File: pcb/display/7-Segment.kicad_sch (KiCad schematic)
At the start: 23 parts, among them J14 XH 2P, J15 XH 2P, J16 XH 2P, J17 XH 2P, J18 XH 2P, J19 XH 2P, J20 XH 2P, Q10 60N03D, Q11 60N03D, Q12 60N03D, Q13 60N03D, Q14 60N03D, Q15 60N03D, Q16 60N03D

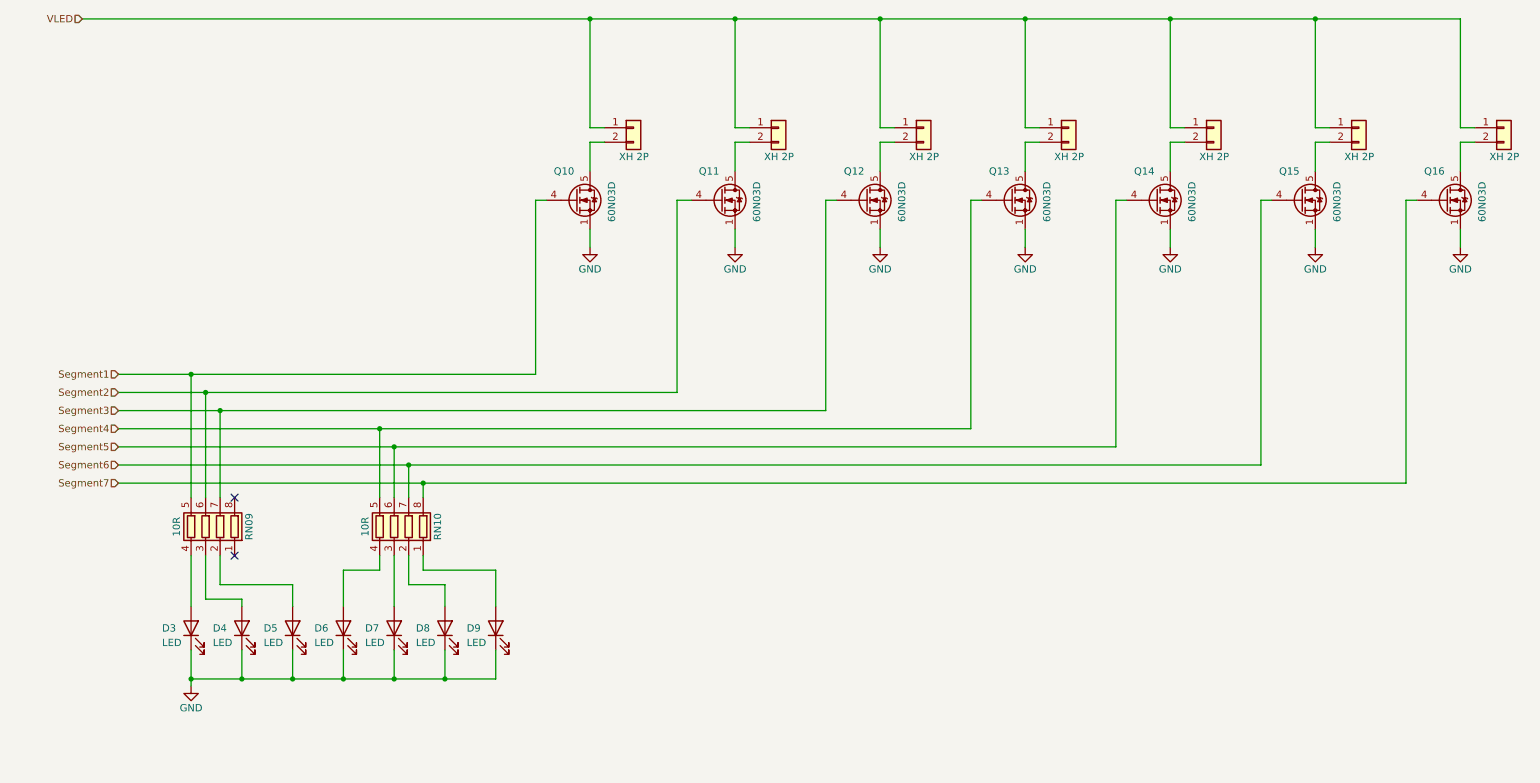
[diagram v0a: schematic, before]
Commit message: Final Version of Prototype Rev. 00
Switched back to PCA9685 for PWM, removed high side switch
Updated some component values
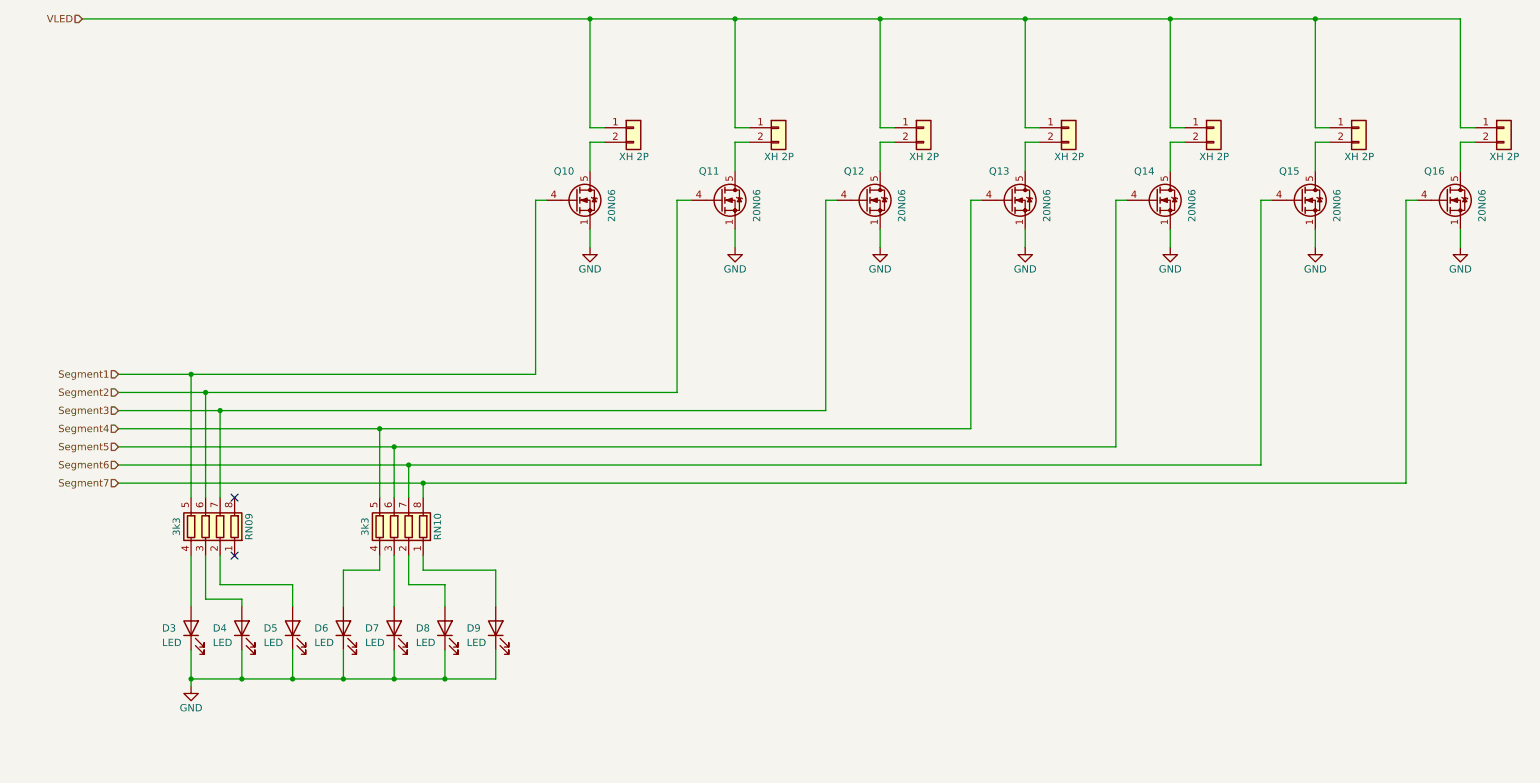
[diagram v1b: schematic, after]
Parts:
- Q10, Q11, Q12, Q13, Q14, Q15, Q16: value 60N03D -> 20N06
- RN09, RN10: value 10R -> 3k3
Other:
- title: (none) -> 7-Segment Driver
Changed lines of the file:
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@@
 	(paper "A4")
 	(title_block
-		(date "2024-11-11")
+		(title "7-Segment Driver")
+		(date "2024-11-17")
 		(rev "00")
 		(company "Ravenspark")
@@
 			)
 		)
-		(property "Value" "60N03D"
+		(property "Value" "20N06"
 			(at 143.51 54.61 90)
 			(effects
@@
 			)
 		)
-		(property "Value" "60N03D"
+		(property "Value" "20N06"
 			(at 168.91 54.61 90)
 			(effects
@@
 			)
 		)
-		(property "Value" "60N03D"
+		(property "Value" "20N06"
 			(at 245.11 54.61 90)
 			(effects
@@
 			)
 		)
-		(property "Value" "60N03D"
+		(property "Value" "20N06"
 			(at 219.71 54.61 90)
 			(effects
@@
 			)
 		)
-		(property "Value" "60N03D"
+		(property "Value" "20N06"
 			(at 270.51 54.61 90)
 			(effects
@@
 			)
 		)
-		(property "Value" "10R"
+		(property "Value" "3k3"
 			(at 74.93 107.95 90)
 			(effects
@@
 			)
 		)
-		(property "Value" "10R"
+		(property "Value" "3k3"
 			(at 41.91 107.95 90)
 			(effects
@@
 			)
 		)
-		(property "Value" "60N03D"
+		(property "Value" "20N06"
 			(at 194.31 54.61 90)
 			(effects
@@
 			)
 		)
-		(property "Value" "60N03D"
+		(property "Value" "20N06"
 			(at 118.11 54.61 90)
 			(effects

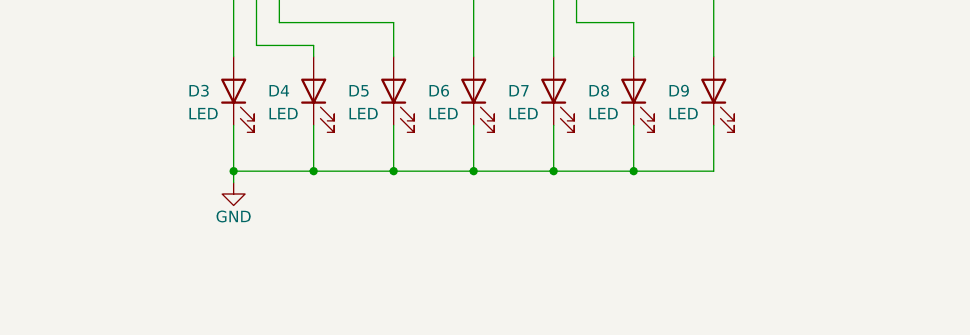
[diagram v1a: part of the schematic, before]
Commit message: Marked known issues in schematic
Add gitignore
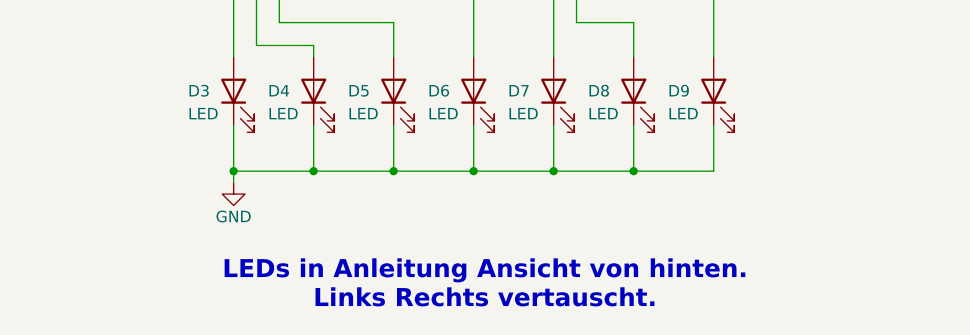
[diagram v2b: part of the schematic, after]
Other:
- note added: "LEDs in Anleitung Ansicht von hinten. Links Rechts vertauscht."
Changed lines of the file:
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@@
+		)
+	)
+	(text "LEDs in Anleitung Ansicht von hinten.\nLinks Rechts vertauscht."
+		(exclude_from_sim no)
+		(at 72.39 147.32 0)
+		(effects
+			(font
+				(size 2 2)
+				(thickness 0.4)
+				(bold yes)
+				(color 255 153 0 1)
+			)
 		)
 	)

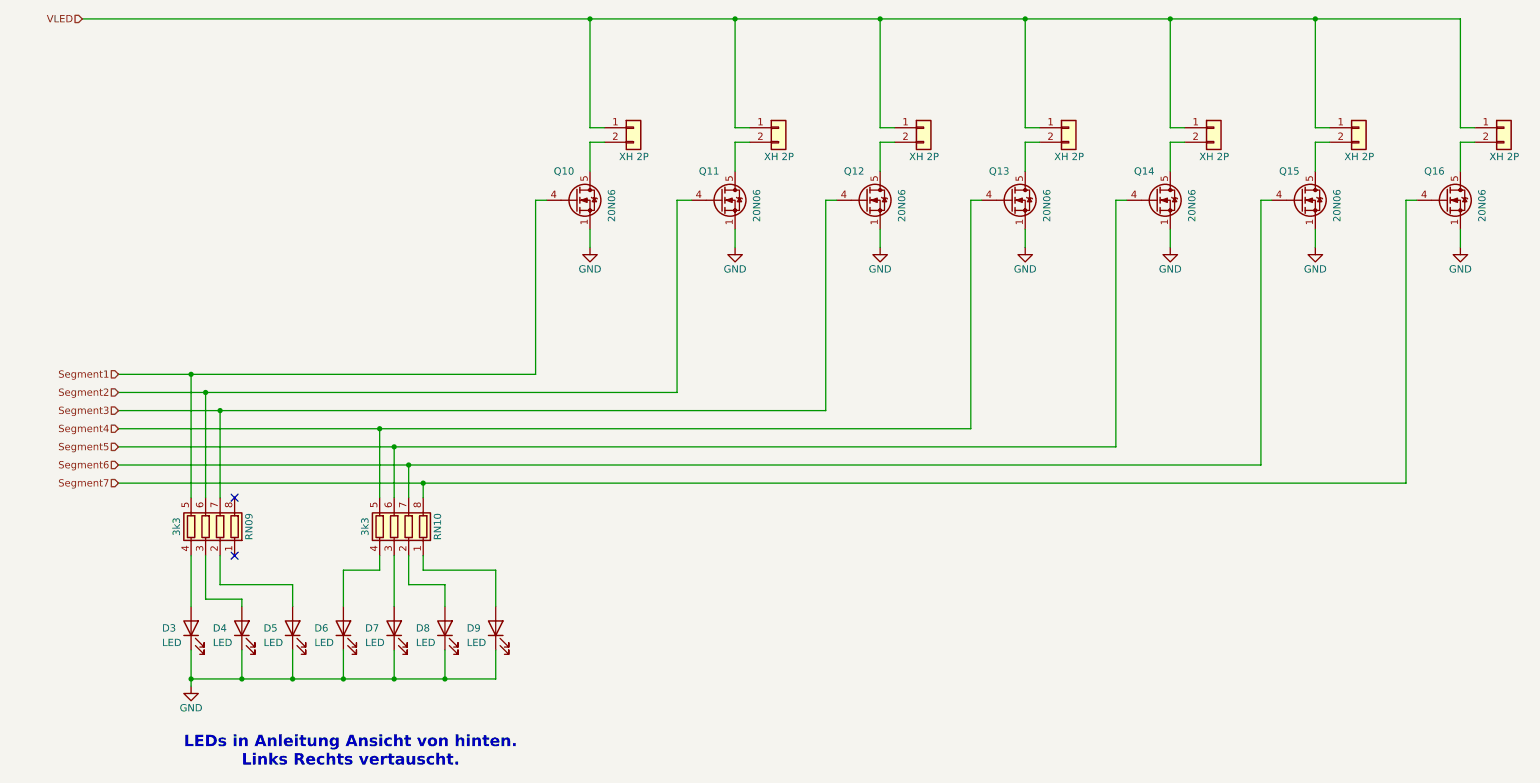
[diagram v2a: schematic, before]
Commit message: Display HW Revision 01
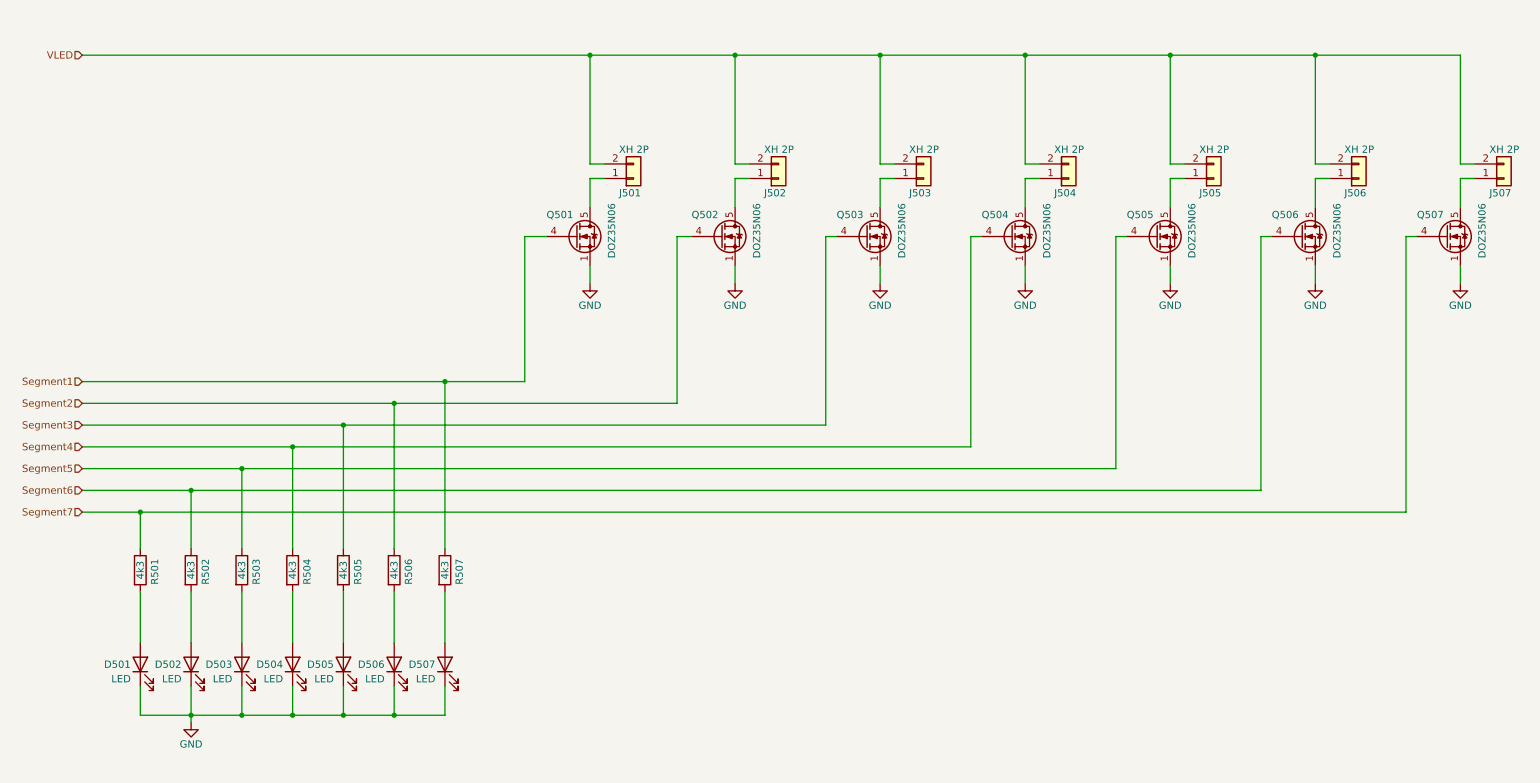
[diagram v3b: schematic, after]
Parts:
- removed RN09, RN10: 3k3, Resistor_SMD:R_Array_Convex_4x0603, symbol Device:R_Pack04
- added R501, R502, R503, R504, R505, R506, R507: 4k3, Resistor_SMD:R_0402_1005Metric, symbol Device:R
- D501: renamed from D9; JLC PN (none) -> C2286
- D502: renamed from D5; JLC PN (none) -> C2286
- D503: renamed from D4; JLC PN (none) -> C2286
- D504: renamed from D3; JLC PN (none) -> C2286
- D505: renamed from D8; JLC PN (none) -> C2286
- D506: renamed from D7; JLC PN (none) -> C2286
- D507: renamed from D6; JLC PN (none) -> C2286
- J501: renamed from J14; JLC PN (none) -> C158012
- J502: renamed from J15; JLC PN (none) -> C158012
- J503: renamed from J16; JLC PN (none) -> C158012
- J504: renamed from J17; JLC PN (none) -> C158012
- J505: renamed from J18; JLC PN (none) -> C158012
- J506: renamed from J19; JLC PN (none) -> C158012
- J507: renamed from J20; JLC PN (none) -> C158012
- Q501: renamed from Q10; value 20N06 -> DOZ35N06; JLC PN (none) -> C36499167
- Q502: renamed from Q11; value 20N06 -> DOZ35N06; JLC PN (none) -> C36499167
- Q503: renamed from Q12; value 20N06 -> DOZ35N06; JLC PN (none) -> C36499167
- Q504: renamed from Q13; value 20N06 -> DOZ35N06; JLC PN (none) -> C36499167
- Q505: renamed from Q14; value 20N06 -> DOZ35N06; JLC PN (none) -> C36499167
- Q506: renamed from Q15; value 20N06 -> DOZ35N06; JLC PN (none) -> C36499167
- Q507: renamed from Q16; value 20N06 -> DOZ35N06; JLC PN (none) -> C36499167
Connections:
- net Segment1: now also R507.1
- net Segment2: now also R506.1
- net Segment3: now also R505.1
- net Segment4: now also R504.1
- net Segment5: now also R503.1
- net Segment6: now also R502.1
- net Segment7: now also R501.1
- net VLED: now also J501.2 (Pin_2), J502.2 (Pin_2), J503.2 (Pin_2), J504.2 (Pin_2), J505.2 (Pin_2), J506.2 (Pin_2), J507.2 (Pin_2); no longer J501.1 (Pin_1), J502.1 (Pin_1), J503.1 (Pin_1), J504.1 (Pin_1), J505.1 (Pin_1), J506.1 (Pin_1), J507.1 (Pin_1)
- net at Q505.5 (D): now also J505.1 (Pin_1); no longer J505.2 (Pin_2)
- net at Q504.5 (D): now also J504.1 (Pin_1); no longer J504.2 (Pin_2)
- net at Q502.5 (D): now also J502.1 (Pin_1); no longer J502.2 (Pin_2)
- net at Q503.5 (D): now also J503.1 (Pin_1); no longer J503.2 (Pin_2)
- net at Q506.5 (D): now also J506.1 (Pin_1); no longer J506.2 (Pin_2)
- net at D504.2 (A): now also R504.2
- net at D506.2 (A): now also R506.2
- net at D507.2 (A): now also R507.2
- net at Q507.5 (D): now also J507.1 (Pin_1); no longer J507.2 (Pin_2)
- net at D503.2 (A): now also R503.2
- net at D501.2 (A): now also R501.2
- net at D505.2 (A): now also R505.2
- net at D502.2 (A): now also R502.2
- net at Q501.5 (D): now also J501.1 (Pin_1); no longer J501.2 (Pin_2)
- no-connect marks 2 -> 0
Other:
- note removed: "LEDs in Anleitung Ansicht von hinten. Links Rechts vertauscht."
- moved on the sheet: D501, D502, D503, D504, D505, D506, D507, Q501, Q502, Q503, Q504, Q505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

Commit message: Conerted to KiCad 9 file version.
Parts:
- renumbered D501 to D401, D502 to D402, D503 to D403, D504 to D404, D505 to D405, D506 to D406, D507 to D407, J501 to J401, J502 to J402, J503 to J403, J504 to J404, J505 to J405, J506 to J406, J507 to J407, Q501 to Q401, Q502 to Q402, Q503 to Q403, Q504 to Q404, Q505 to Q405, Q506 to Q406, Q507 to Q407, R501 to R401, R502 to R402, R503 to R403, R504 to R404, R505 to R405, R506 to R406, R507 to R407
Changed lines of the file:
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@@
 (kicad_sch
-	(version 20231120)
+	(version 20250114)
 	(generator "eeschema")
-	(generator_version "8.0")
+	(generator_version "9.0")
 	(paper "A4")
 	(title_block
@@
 		(shape input)
 		(at 25.4 101.6 180)
-		(fields_autoplaced yes)
 		(effects
 			(font
@@
 		(shape input)
 		(at 25.4 97.79 180)
-		(fields_autoplaced yes)
 		(effects
 			(font
@@
 		(shape input)
 		(at 25.4 105.41 180)
-		(fields_autoplaced yes)
 		(effects
 			(font
@@
 		(shape input)
 		(at 25.4 90.17 180)
-		(fields_autoplaced yes)
 		(effects
 			(font
@@
 		(shape input)
 		(at 25.4 93.98 180)
-		(fields_autoplaced yes)
 		(effects
 			(font
@@
 		(shape input)
 		(at 25.4 86.36 180)
-		(fields_autoplaced yes)
 		(effects
 			(font
@@
 		(shape input)
 		(at 25.4 82.55 180)
-		(fields_autoplaced yes)
 		(effects
 			(font
@@
 		(shape input)
 		(at 25.4 25.4 180)
-		(fields_autoplaced yes)
 		(effects
 			(font
@@
 		(on_board yes)
 		(dnp no)
-		(property "Reference" "R501"
+		(property "Reference" "R401"
 			(at 38.1 118.11 90)
 			(effects
@@
 		(on_board yes)
 		(dnp no)
-		(property "Reference" "J505"
+		(property "Reference" "J405"
 			(at 220.98 49.53 0)
 			(effects
@@
 		(on_board yes)
 		(dnp no)
-		(property "Reference" "J504"
+		(property "Reference" "J404"
 			(at 195.58 49.53 0)
 			(effects
@@
 		(on_board yes)
 		(dnp no)
-		(property "Reference" "#PWR0504"
+		(property "Reference" "#PWR0404"
 			(at 190.5 71.755 0)
 			(effects
@@
 		(on_board yes)
 		(dnp no)
-		(property "Reference" "R502"
+		(property "Reference" "R402"
 			(at 46.99 118.11 90)
 			(effects
@@
 		(on_board yes)
 		(dnp no)
-		(property "Reference" "Q502"
+		(property "Reference" "Q402"
 			(at 132.08 53.34 0)
 			(effects
@@
 		(on_board yes)
 		(dnp no)
-		(property "Reference" "Q503"
+		(property "Reference" "Q403"
 			(at 157.48 53.34 0)
 			(effects
@@
 		(on_board yes)
 		(dnp no)
-		(property "Reference" "Q506"
+		(property "Reference" "Q406"
 			(at 233.68 53.34 0)
 			(effects
@@
 		(on_board yes)
 		(dnp no)
-		(property "Reference" "#PWR0503"
+		(property "Reference" "#PWR0403"
 			(at 165.1 71.755 0)
 			(effects
@@
 		(on_board yes)
 		(dnp no)
-		(property "Reference" "D504"
+		(property "Reference" "D404"
 			(at 55.88 132.08 90)
 			(effects
@@
 		(on_board yes)
 		(dnp no)
-		(property "Reference" "R505"
+		(property "Reference" "R405"
 			(at 73.66 118.11 90)
 			(effects
@@
 		(on_board yes)
 		(dnp no)
-		(property "Reference" "#PWR0502"
+		(property "Reference" "#PWR0402"
 			(at 139.7 71.755 0)
 			(effects
@@
 		(on_board yes)
 		(dnp no)
-		(property "Reference" "D506"
+		(property "Reference" "D406"
 			(at 73.66 132.08 90)
 			(effects
@@
 		(on_board yes)
 		(dnp no)
-		(property "Reference" "D507"
+		(property "Reference" "D407"
 			(at 82.55 132.08 90)
 			(effects
@@
 		(on_board yes)
 		(dnp no)
-		(property "Reference" "Q505"
+		(property "Reference" "Q405"
 			(at 208.28 53.34 0)
 			(effects
@@
 		(on_board yes)
 		(dnp no)
-		(property "Reference" "J502"
+		(property "Reference" "J402"
 			(at 144.78 49.53 0)
 			(effects
@@
 		(on_board yes)
 		(dnp no)
-		(property "Reference" "Q507"
+		(property "Reference" "Q407"
 			(at 259.08 53.34 0)
 			(effects
@@
 		(on_board yes)
 		(dnp no)
-		(property "Reference" "D503"
+		(property "Reference" "D403"
 			(at 46.99 132.08 90)
 			(effects
@@
 		(on_board yes)
 		(dnp no)
-		(property "Reference" "#PWR0507"
+		(property "Reference" "#PWR0407"
 			(at 266.7 71.755 0)
 			(effects
@@
 		(on_board yes)
 		(dnp no)
-		(property "Reference" "R504"
+		(property "Reference" "R404"
 			(at 64.77 118.11 90)
 			(effects
@@
 		(on_board yes)
 		(dnp no)
-		(property "Reference" "Q504"
+		(property "Reference" "Q404"
 			(at 182.88 53.34 0)
 			(effects
@@
 		(on_board yes)
 		(dnp no)
-		(property "Reference" "J506"
+		(property "Reference" "J406"
 			(at 246.38 49.53 0)
 			(effects
@@
 		(on_board yes)
 		(dnp no)
-		(property "Reference" "#PWR0506"
+		(property "Reference" "#PWR0406"
 			(at 241.3 71.755 0)
 			(effects
@@
 		(on_board yes)
 		(dnp no)
-		(property "Reference" "#PWR0508"
+		(property "Reference" "#PWR0408"
 			(at 44.45 148.59 0)
 			(effects
@@
 		(on_board yes)
 		(dnp no)
-		(property "Reference" "R507"
+		(property "Reference" "R407"
 			(at 91.44 118.11 90)
 			(effects
@@
 		(on_board yes)
 		(dnp no)
-		(property "Reference" "D505"
+		(property "Reference" "D405"
 			(at 64.77 132.08 90)
 			(effects
@@
 		(on_board yes)
 		(dnp no)
-		(property "Reference" "D501"
+		(property "Reference" "D401"
 			(at 29.21 132.08 90)
 			(effects
@@
 		(on_board yes)
 		(dnp no)
-		(property "Reference" "J507"
+		(property "Reference" "J407"
 			(at 271.78 49.53 0)
 			(effects
@@
 		(on_board yes)
 		(dnp no)
-		(property "Reference" "#PWR0501"
+		(property "Reference" "#PWR0401"
 			(at 114.3 71.755 0)
 			(effects
@@
 		(on_board yes)
 		(dnp no)
-		(property "Reference" "J501"
+		(property "Reference" "J401"
 			(at 119.38 49.53 0)
 			(effects
@@
 		(on_board yes)
 		(dnp no)
-		(property "Reference" "Q501"
+		(property "Reference" "Q401"
 			(at 106.68 53.34 0)
 			(effects
@@
 		(on_board yes)
 		(dnp no)
-		(property "Reference" "R503"
+		(property "Reference" "R403"
 			(at 55.88 118.11 90)
 			(effects
@@
 		(on_board yes)
 		(dnp no)
-		(property "Reference" "J503"
+		(property "Reference" "J403"
 			(at 170.18 49.53 0)
 			(effects
@@
 		(on_board yes)
 		(dnp no)
-		(property "Reference" "R506"
+		(property "Reference" "R406"
 			(at 82.55 118.11 90)
 			(effects
@@
 		(on_board yes)
 		(dnp no)
-		(property "Reference" "D502"
+		(property "Reference" "D402"
 			(at 38.1 132.08 90)
 			(effects
@@
 		(on_board yes)
 		(dnp no)
-		(property "Reference" "#PWR0505"
+		(property "Reference" "#PWR0405"
 			(at 215.9 71.755 0)
 			(effects
